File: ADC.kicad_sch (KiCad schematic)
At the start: 17 parts, among them U16 AD9218BSTZ-105

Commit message: decided on clk source and MCU
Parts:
- removed R97: 0R, Resistor_SMD:R_0603_1608Metric_Pad0.98x0.95mm_HandSolder, symbol Device:R
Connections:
- net ENCB is gone; now on net ENC: U16.14 (ENCB)
- net ENCA renamed ENC
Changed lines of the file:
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@@
-	)
-	(junction
-		(at 134.62 91.44)
-		(diameter 0)
-		(color 0 0 0 0)
 	)
 	(junction
@@
 	)
 	(junction
+		(at 182.88 93.98)
+		(diameter 0)
+		(color 0 0 0 0)
+	)
+	(junction
 		(at 100.33 146.05)
 		(diameter 0)
@@
 	(junction
 		(at 182.88 129.54)
-		(diameter 0)
-		(color 0 0 0 0)
-	)
-	(junction
-		(at 134.62 99.06)
 		(diameter 0)
 		(color 0 0 0 0)
@@
 	(wire
 		(pts
-			(xy 132.08 99.06) (xy 134.62 99.06)
-		)
-		(stroke
-			(width 0)
-			(type default)
-		)
-	)
-	(wire
-		(pts
 			(xy 113.03 146.05) (xy 125.73 146.05)
 		)
@@
 	(wire
 		(pts
-			(xy 134.62 91.44) (xy 142.24 91.44)
-		)
-		(stroke
-			(width 0)
-			(type default)
-		)
-	)
-	(wire
-		(pts
 			(xy 182.88 127) (xy 182.88 124.46)
 		)
@@
 	(wire
 		(pts
+			(xy 180.34 93.98) (xy 182.88 93.98)
+		)
+		(stroke
+			(width 0)
+			(type default)
+		)
+	)
+	(wire
+		(pts
 			(xy 156.21 99.06) (xy 148.59 99.06)
 		)
@@
 	(wire
 		(pts
-			(xy 142.24 96.52) (xy 185.42 96.52)
-		)
-		(stroke
-			(width 0)
-			(type default)
-		)
-	)
-	(wire
-		(pts
 			(xy 182.88 127) (xy 185.42 127)
 		)
@@
 		)
 	)
-	(wire
-		(pts
-			(xy 132.08 91.44) (xy 134.62 91.44)
-		)
-		(stroke
-			(width 0)
-			(type default)
-		)
-	)
 	(bus
 		(pts
@@
 	(wire
 		(pts
-			(xy 142.24 99.06) (xy 142.24 96.52)
+			(xy 185.42 96.52) (xy 182.88 96.52)
 		)
 		(stroke
@@
 	(wire
 		(pts
-			(xy 134.62 99.06) (xy 142.24 99.06)
+			(xy 182.88 93.98) (xy 185.42 93.98)
 		)
 		(stroke
@@
 	(wire
 		(pts
-			(xy 142.24 91.44) (xy 142.24 93.98)
-		)
-		(stroke
-			(width 0)
-			(type default)
-		)
-	)
-	(wire
-		(pts
 			(xy 125.73 133.35) (xy 138.43 133.35)
 		)
@@
 	(wire
 		(pts
+			(xy 182.88 96.52) (xy 182.88 93.98)
+		)
+		(stroke
+			(width 0)
+			(type default)
+		)
+	)
+	(wire
+		(pts
 			(xy 125.73 130.81) (xy 125.73 133.35)
 		)
@@
 		(pts
 			(xy 163.83 99.06) (xy 182.88 99.06)
-		)
-		(stroke
-			(width 0)
-			(type default)
-		)
-	)
-	(wire
-		(pts
-			(xy 142.24 93.98) (xy 185.42 93.98)
 		)
 		(stroke
@@
 		)
 	)
+	(hierarchical_label "ENC"
+		(shape input)
+		(at 180.34 93.98 180)
+		(effects
+			(font
+				(size 1.27 1.27)
+			)
+			(justify right)
+		)
+	)
 	(hierarchical_label "VCM_out"
 		(shape output)
@@
 		)
 	)
-	(hierarchical_label "ENCB"
-		(shape input)
-		(at 132.08 99.06 180)
-		(effects
-			(font
-				(size 1.27 1.27)
-			)
-			(justify right)
-		)
-	)
 	(hierarchical_label "INA_N"
 		(shape input)
 		(at 180.34 109.22 180)
-		(effects
-			(font
-				(size 1.27 1.27)
-			)
-			(justify right)
-		)
-	)
-	(hierarchical_label "ENCA"
-		(shape input)
-		(at 132.08 91.44 180)
 		(effects
 			(font
@@
 					(unit 1)
 				)
-			)
-		)
-	)
-	(symbol
-		(lib_id "Device:R")
-		(at 134.62 95.25 0)
-		(unit 1)
-		(exclude_from_sim no)
-		(in_bom yes)
-		(on_board yes)
-		(dnp no)
-		(fields_autoplaced yes)
-		(property "Reference" "R97"
-			(at 137.16 93.9799 0)
-			(effects
-				(font
-					(size 1.27 1.27)
-				)
-				(justify left)
-			)
-		)
-		(property "Value" "0R"
-			(at 137.16 96.5199 0)
-			(effects
-				(font
-					(size 1.27 1.27)
-				)
-				(justify left)
-			)
-		)
-		(property "Footprint" "Resistor_SMD:R_0603_1608Metric_Pad0.98x0.95mm_HandSolder"
-			(at 132.842 95.25 90)
-			(effects
-				(font
-					(size 1.27 1.27)
-				)
-				(hide yes)
-			)
-		)
-		(property "Datasheet" "~"
-			(at 134.62 95.25 0)
-			(effects
-				(font
-					(size 1.27 1.27)
-				)
-				(hide yes)
-			)
-		)
-		(property "Description" "Resistor"
-			(at 134.62 95.25 0)
-			(effects
-				(font
-					(size 1.27 1.27)
-				)
-				(hide yes)
-			)
-		)
-		(pin "1"
-		)
-		(pin "2"
-		)
-		(instances
-			(project "thunderscope-lite"
-				(path "/920a8b65-6ec2-414c-bfee-6322de42233d/6746a992-99cd-4d6d-8c54-ccff196b517b"
-					(reference "R97")
-					(unit 1)
-				)

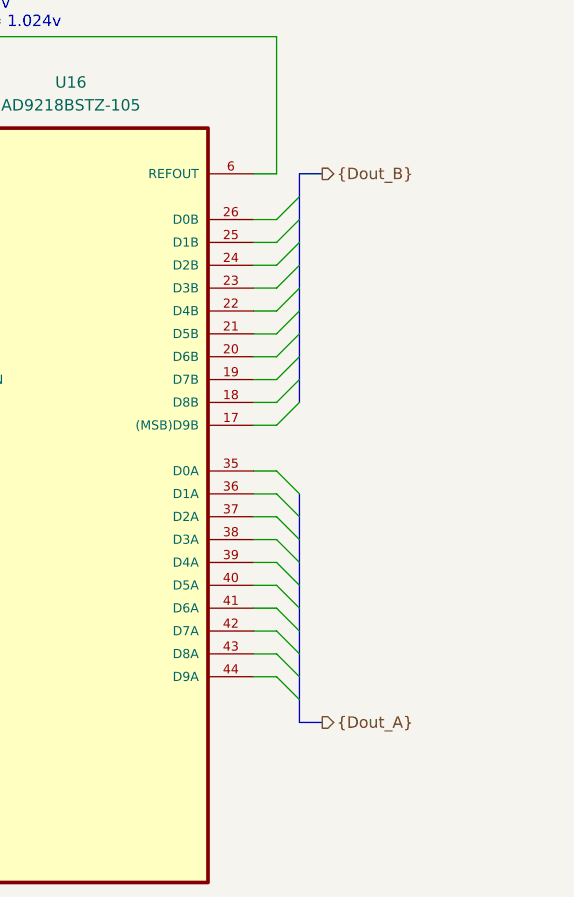
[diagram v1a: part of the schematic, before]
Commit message: schematic complete. no ERC errors
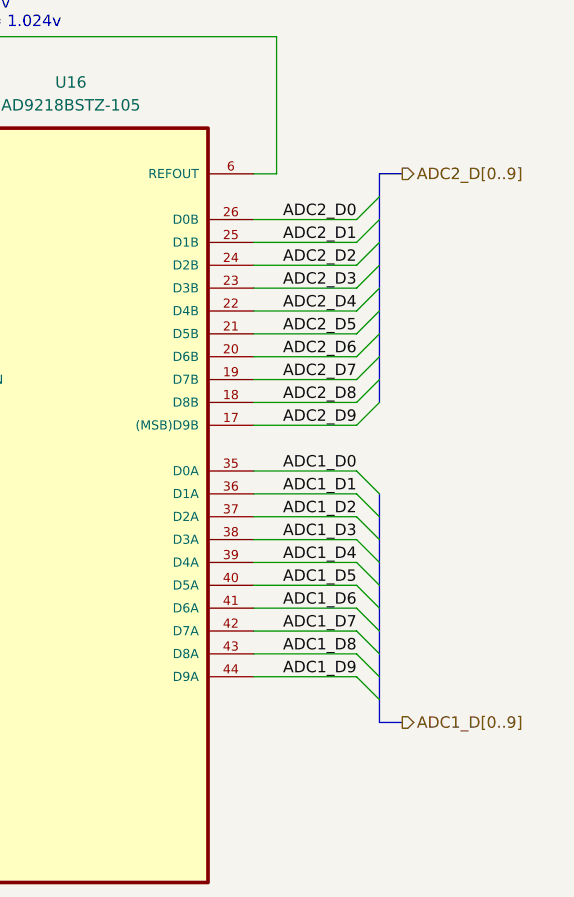
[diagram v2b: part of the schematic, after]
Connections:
- net ADC2_D9: now reaches U16.17 ((MSB)D9B)
- net ADC2_D8: now reaches U16.18 (D8B)
- net ADC2_D7: now reaches U16.19 (D7B)
- net ADC2_D6: now reaches U16.20 (D6B)
- net ADC2_D5: now reaches U16.21 (D5B)
- net ADC2_D4: now reaches U16.22 (D4B)
- net ADC2_D3: now reaches U16.23 (D3B)
- net ADC2_D2: now reaches U16.24 (D2B)
- net ADC2_D1: now reaches U16.25 (D1B)
- net ADC2_D0: now reaches U16.26 (D0B)
- net ADC1_D0: now reaches U16.35 (D0A)
- net ADC1_D1: now reaches U16.36 (D1A)
- net ADC1_D2: now reaches U16.37 (D2A)
- net ADC1_D3: now reaches U16.38 (D3A)
- net ADC1_D4: now reaches U16.39 (D4A)
- net ADC1_D5: now reaches U16.40 (D5A)
- net ADC1_D6: now reaches U16.41 (D6A)
- net ADC1_D7: now reaches U16.42 (D7A)
- net ADC1_D8: now reaches U16.43 (D8A)
- net ADC1_D9: now reaches U16.44 (D9A)
